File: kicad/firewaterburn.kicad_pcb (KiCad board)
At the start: 4 copper layers, 90 x 50 mm, 83 parts, among them J201 AudioJack2_SwitchT, J202 AudioJack2_SwitchT, J203 AudioJack2_SwitchT, J204 AudioJack2_SwitchT, J205 AudioJack2_SwitchT, J206 AudioJack2_SwitchT, J207 Conn_01x03, J301 Conn_01x05, J302 TC-2050, J501 RVT50HQBNWC00, P101 USB_C_Plug_USB2.0, Q201 DMP31D0U-7, Q202 DMN61D9UWQ-13, Q401 SI7421DN-T1-E3, U101 TPD4E02B04DQA, U301 BL654, U401 LT3973-3.3, U402 STUSB4500QTR, U403 LM2775DSG, Y301 Crystal

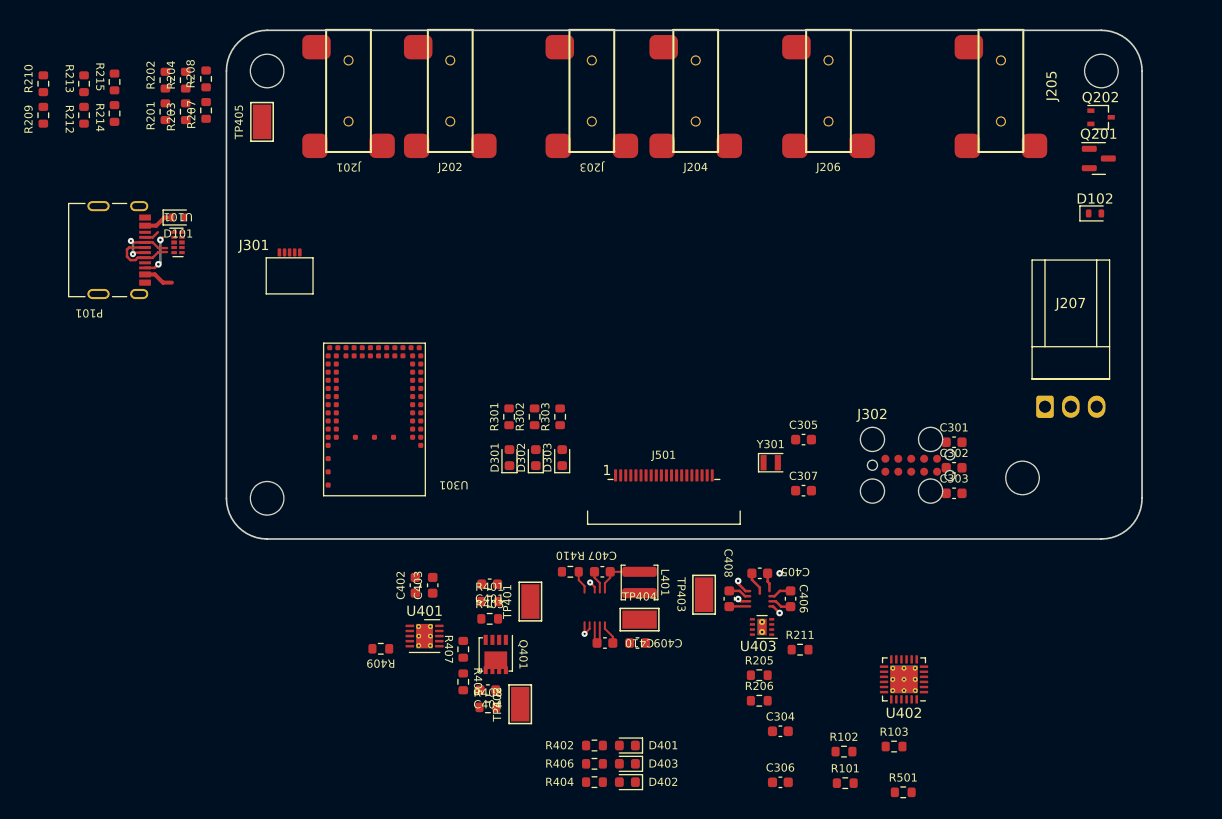
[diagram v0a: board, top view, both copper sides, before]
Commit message: add nrf52840 board
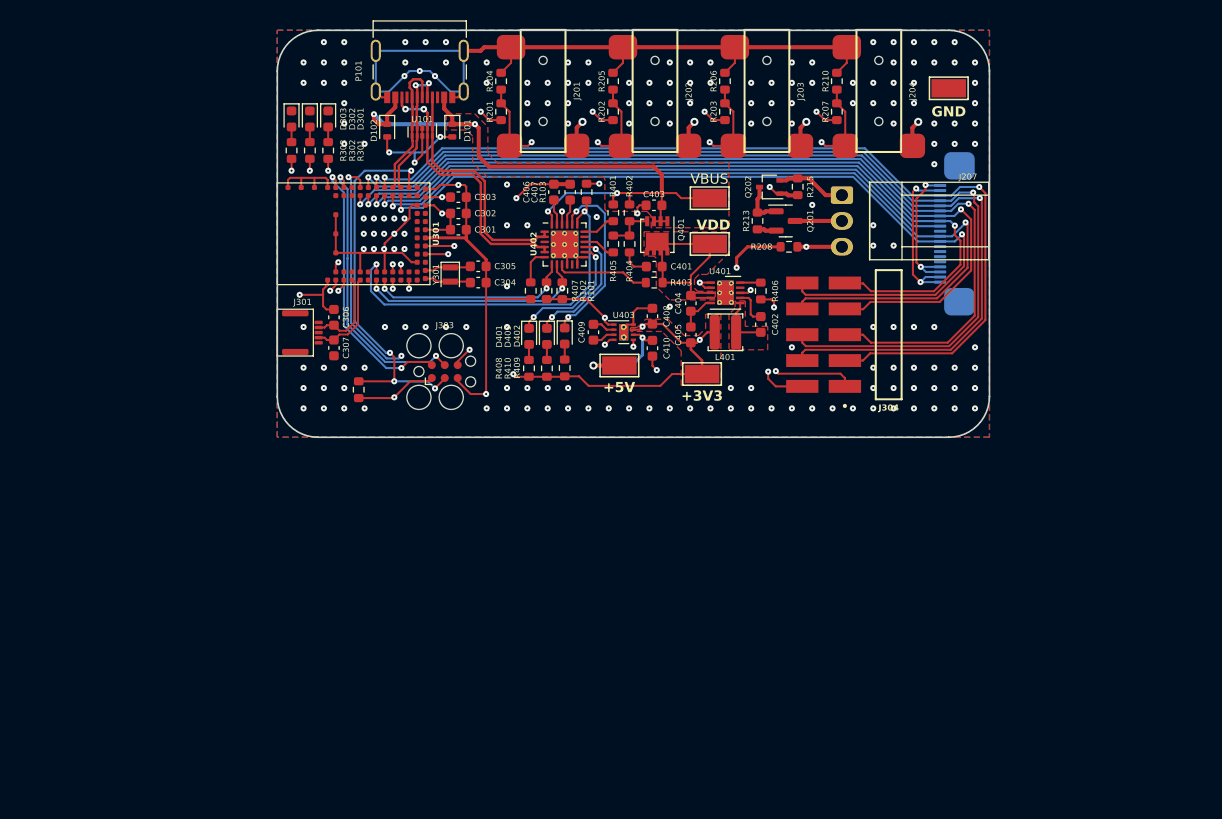
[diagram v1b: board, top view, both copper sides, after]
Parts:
- removed J205, J206: AudioJack2_SwitchT, mylib_connector:MJ-2523
- removed J302: TC-2050, mylib_connector:TC-2050
- removed R209: 4k42, Resistor_SMD:R_0603_1608Metric
- removed R211, R212: 3k4, Resistor_SMD:R_0603_1608Metric
- removed R214: 10k, Resistor_SMD:R_0603_1608Metric
- removed R501: 0R, Resistor_SMD:R_0603_1608Metric
- added J303: Conn_ARM_SWD_TagConnect_TC2030, Connector:Tag-Connect_TC2030-IDC-FP_2x03_P1.27mm_Vertical, F.Cu at (116.5, 93.5)
- added J304: TSM-105-01-L-DH, mylib_connector:SAMTEC_TSM-105-01-L-DH, F.Cu at (160.1, 89.9)
- added R305: 4k7, Resistor_SMD:R_0603_1608Metric, F.Cu at (108.0, 95.3)
- J501: moved to B.Cu
- R208: value 4k42 -> 4k7
- U301: footprint mylib_ic:BL654 -> mylib_ic:BL654-00001
- moved R210 78.0 mm to (155.0, 65.0)
- moved D102 70.1 mm to (110.8, 69.8), turned to -90 degrees
- moved R215 67.9 mm to (151.2, 75.4)
- moved R213 67.6 mm to (147.2, 78.7)
- moved TP401 65.1 mm to (166.0, 65.7), turned to 0 degrees
- moved C306 63.4 mm to (105.6, 88.2), turned to 90 degrees
- moved R103 62.3 mm to (130.4, 75.9), turned to -90 degrees
- moved R207 62.0 mm to (155.0, 68.0)
- moved R206 61.0 mm to (144.0, 65.0), turned to 90 degrees
- moved R205 60.1 mm to (133.0, 65.0), turned to 90 degrees
- moved R208 59.6 mm to (150.3, 81.3), turned to 0 degrees
- moved C303 56.8 mm to (117.8, 76.4)
- moved R101 55.8 mm to (128.0, 85.6), turned to 90 degrees
- moved C302 54.8 mm to (117.8, 78.0)
- moved U402 54.2 mm to (128.2, 81.0), turned to 0 degrees
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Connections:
- net Net-(J301-Pin_2) renamed /mcu_n_tft/NFC+
- net Net-(J301-Pin_4) renamed /mcu_n_tft/NFC-
- J501 pad 1: Net-(J501-VDD) -> +3V3
- J501 pad 17: Net-(J501-VDD) -> +3V3
- J501 pad 18: Net-(J501-VDD) -> +3V3
- R208 pad 2: /OUTPUT/probe4 -> /OUTPUT/TACHO
- R301 pad 2: Net-(U301-P0.17) -> /mcu_n_tft/LED1
- R302 pad 2: Net-(U301-P0.15) -> /mcu_n_tft/LED2
- R303 pad 2: Net-(U301-P0.13) -> /mcu_n_tft/LED3
- U301 pad 10: unconnected-(U301-P0.24-Pad10) -> /mcu_n_tft/~{INT}
- U301 pad 11: unconnected-(U301-P0.22-Pad11) -> /mcu_n_tft/QSPI_IO1
- U301 pad 12: unconnected-(U301-P0.21-Pad12) -> /mcu_n_tft/~{PD}
- U301 pad 13: unconnected-(U301-P0.20-Pad13) -> /mcu_n_tft/QSPI_CLK
- U301 pad 14: unconnected-(U301-P0.19-Pad14) -> /mcu_n_tft/GPIO0
- U301 pad 16: Net-(U301-P0.17) -> /mcu_n_tft/QSPI_IO2
- U301 pad 18: Net-(U301-P0.15) -> /mcu_n_tft/QSPI_IO3
- U301 pad 19: /mcu_n_tft/Reset -> /mcu_n_tft/~{Reset}
- U301 pad 2: /mcu_n_tft/SCL -> unconnected-(U301-P1.04-Pad2)
- U301 pad 20: Net-(U301-P0.13) -> unconnected-(U301-P0.13-Pad20)
- U301 pad 21: /mcu_n_tft/GPIO0 -> unconnected-(U301-P0.16-Pad21)
- U301 pad 22: /mcu_n_tft/~{PD} -> unconnected-(U301-P0.14-Pad22)
- U301 pad 27: /mcu_n_tft/~{INT} -> unconnected-(U301-P0.11-Pad27)
- U301 pad 28: /mcu_n_tft/QSPI_CLK -> unconnected-(U301-P0.12-Pad28)
- U301 pad 29: /mcu_n_tft/QSPI_~{CS} -> unconnected-(U301-P0.08-Pad29)
- U301 pad 30: /mcu_n_tft/I2C_INT -> unconnected-(U301-P1.09-Pad30)
- U301 pad 34: /OUTPUT/probe3 -> /OUTPUT/probe4
- U301 pad 35: /mcu_n_tft/QSPI_IO3 -> /OUTPUT/PWM
- U301 pad 36: /mcu_n_tft/QSPI_IO2 -> unconnected-(U301-P0.26-Pad36)
- U301 pad 37: /mcu_n_tft/QSPI_IO1 -> /OUTPUT/TACHO
- U301 pad 38: /mcu_n_tft/QSPI_IO0 -> unconnected-(U301-P0.27-Pad38)
- U301 pad 39: /OUTPUT/probe4 -> /OUTPUT/probe5
- U301 pad 4: /mcu_n_tft/SDA -> unconnected-(U301-P1.02-Pad4)
- U301 pad 44: /mcu_n_tft/ADC_7 -> /OUTPUT/probe7
- U301 pad 45: /OUTPUT/probe7 -> /OUTPUT/probe3
- U301 pad 46: /OUTPUT/probe5 -> /OUTPUT/probe6
- U301 pad 48: /OUTPUT/probe6 -> /OUTPUT/probe1
- U301 pad 5: /OUTPUT/TACHO -> unconnected-(U301-P1.03-Pad5)
- U301 pad 50: /OUTPUT/probe1 -> /OUTPUT/probe0
- U301 pad 51: unconnected-(U301-P1.14-Pad51) -> /mcu_n_tft/SCL
- U301 pad 53: unconnected-(U301-P1.15-Pad53) -> /mcu_n_tft/SDA
- U301 pad 54: unconnected-(U301-P1.12-Pad54) -> /mcu_n_tft/I2C_INT
- U301 pad 6: /OUTPUT/PWM -> unconnected-(U301-P1.01-Pad6)
- U301 pad 61: unconnected-(U301-P1.05-Pad61) -> /mcu_n_tft/LED3
- U301 pad 63: unconnected-(U301-P1.06-Pad63) -> /mcu_n_tft/LED2
- U301 pad 64: unconnected-(U301-P1.07-Pad64) -> /mcu_n_tft/LED1
- U301 pad 8: unconnected-(U301-P0.25-Pad8) -> /mcu_n_tft/QSPI_~{CS}
- U301 pad 9: unconnected-(U301-P0.23-Pad9) -> /mcu_n_tft/QSPI_IO0
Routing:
- net GND: track 9.05 -> 240.5 mm, vias 0 -> 194
- net +3V3: track 29.3 -> 231.3 mm, vias 6 -> 19
- net /mcu_n_tft/QSPI_IO0: track 0.00 -> 96.8 mm, vias 0 -> 2
- net /mcu_n_tft/QSPI_IO1: track 0.00 -> 95.3 mm, vias 0 -> 2
- net /mcu_n_tft/QSPI_CLK: track 0.00 -> 91.9 mm, vias 0 -> 2
- net /mcu_n_tft/QSPI_~{CS}: track 0.00 -> 90.3 mm, vias 0 -> 2
- net /mcu_n_tft/QSPI_IO2: track 0.00 -> 84.8 mm, vias 0 -> 2
- net /mcu_n_tft/~{INT}: track 0.00 -> 83.6 mm, vias 0 -> 2
- net /mcu_n_tft/QSPI_IO3: track 0.00 -> 82.0 mm, vias 0 -> 2
- net /mcu_n_tft/~{PD}: track 0.00 -> 78.5 mm, vias 0 -> 2
- net VBUS: track 5.93 -> 69.0 mm, vias 0 -> 4
- net /OUTPUT/probe3: track 0.00 -> 61.1 mm, vias 0 -> 2
- net /mcu_n_tft/GPIO0: track 0.00 -> 59.2 mm, vias 0 -> 1
- net /mcu_n_tft/SDA: track 0.00 -> 54.9 mm, vias 0 -> 3
- net /OUTPUT/probe2: track 0.00 -> 51.1 mm, vias 0 -> 2
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- added copper zone on F.Cu, net +3V3
- added copper zone on In2.Cu, net +3V3
- added copper zone on B.Cu, net GND
- added copper zone on F.Cu, net GND
- added copper zone on In1.Cu, net GND
- added copper zone on In2.Cu, net GND
- added copper zone on F.Cu, net Net-(U401-SW)
- added copper zone on F.Cu, net VBUS
- added copper zone on F.Cu, net VDD
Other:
- board size 90 x 50 mm -> 70 x 40 mm
- board text added: "+3V3"
- board text added: "+5V"
- board text added: "GND"
- board text added: "VBUS"
- board text added: "VDD"

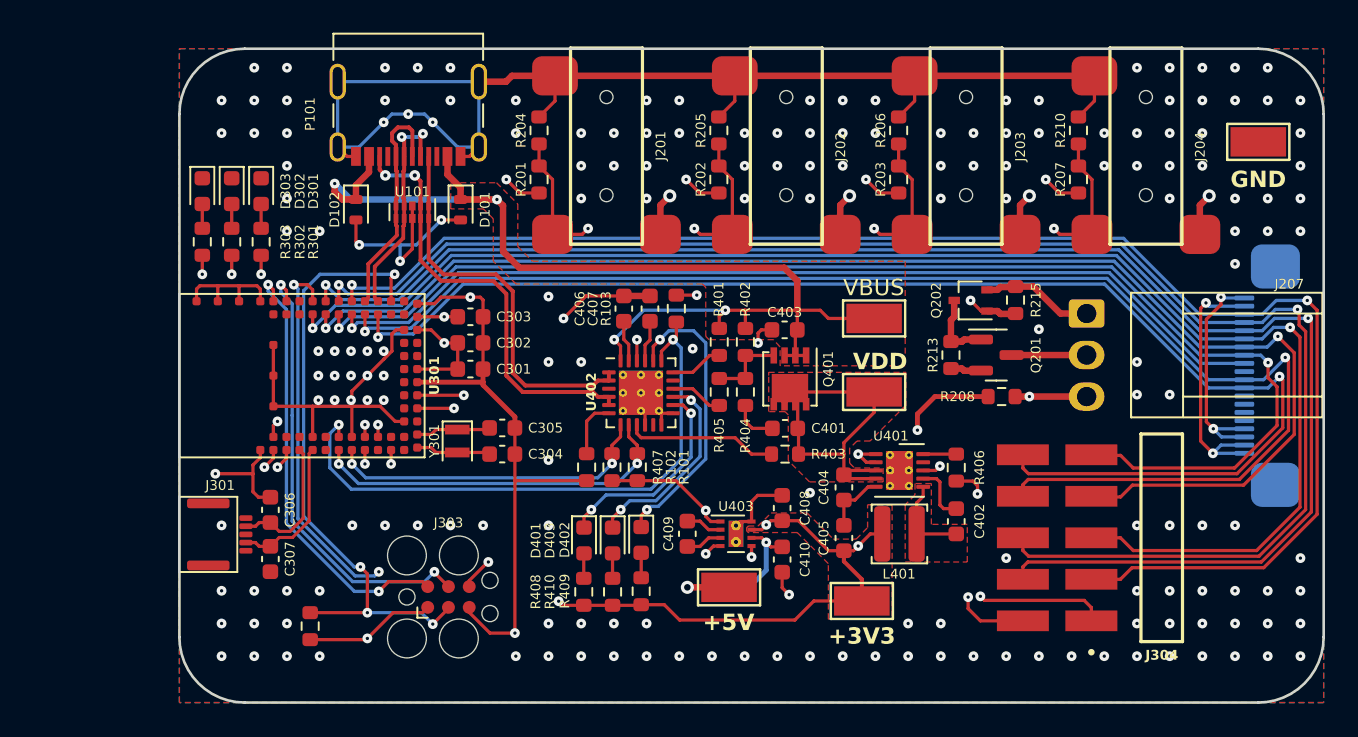
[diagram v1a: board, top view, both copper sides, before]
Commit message: rework board
add nrf 7002
add oled display
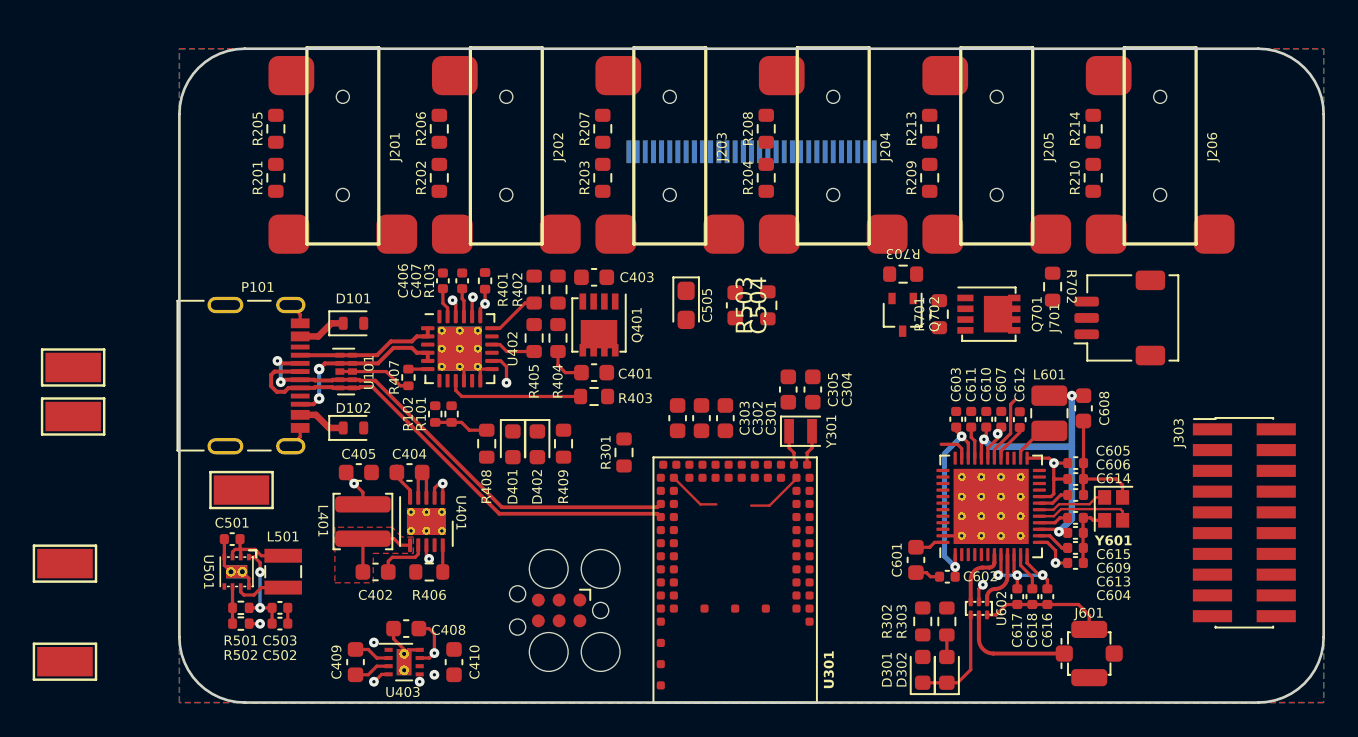
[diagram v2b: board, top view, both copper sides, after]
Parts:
- removed C306, C307: 300p, Capacitor_SMD:C_0603_1608Metric
- removed D303, D403: LED, LED_SMD:LED_0603_1608Metric
- removed J207: Conn_01x03, mylib_connector:Molex_KK-254_AE-6410-03A_1x03_P2.54mm_Vertical
- removed J304: TSM-105-01-L-DH, mylib_connector:SAMTEC_TSM-105-01-L-DH
- removed Q201: DMP31D0U-7, Package_TO_SOT_SMD:SOT-23
- removed Q202: DMN61D9UWQ-13, Package_TO_SOT_SMD:SOT-323_SC-70
- removed R215, R305: 4k7, Resistor_SMD:R_0603_1608Metric
- removed R410: 1k, Resistor_SMD:R_0603_1608Metric
- added C501: 1µ, Capacitor_SMD:C_0402_1005Metric, F.Cu at (103.2, 90.0)
- added C502: 10µ, Capacitor_SMD:C_0402_1005Metric, F.Cu at (106.2, 95.2)
- added C503: 100nF, Capacitor_SMD:C_0402_1005Metric, F.Cu at (106.2, 94.2)
- added C504: 100nF, Capacitor_SMD:C_0603_1608Metric, F.Cu at (134.0, 75.7)
- added C505: 4µ7, Capacitor_Tantalum_SMD:CP_EIA-2012-15_AVX-P, F.Cu at (131.0, 75.7)
- added C601: 2µ2, Capacitor_SMD:C_0603_1608Metric, F.Cu at (145.1, 91.3)
- added C602: 100n, Capacitor_SMD:C_0402_1005Metric, F.Cu at (147.0, 92.3)
- added C603: 2µ2, Capacitor_SMD:C_0402_1005Metric, F.Cu at (147.5, 82.7)
- added C604: 4µ7, Capacitor_SMD:C_0402_1005Metric, F.Cu at (154.8, 91.5)
- added C605: 4µ7, Capacitor_SMD:C_0402_1005Metric, F.Cu at (154.8, 85.3)
- added C606: 1µ, Capacitor_SMD:C_0402_1005Metric, F.Cu at (154.8, 86.3)
- added C607: 2µ2, Capacitor_SMD:C_0402_1005Metric, F.Cu at (150.3, 82.7)
- added C608: 4µ7, Capacitor_SMD:C_0603_1608Metric, F.Cu at (155.3, 82.0)
- added C609: 0.22µ, Capacitor_SMD:C_0402_1005Metric, F.Cu at (154.8, 89.6)
- added C610: 0.47µ, Capacitor_SMD:C_0402_1005Metric, F.Cu at (149.4, 82.7)
- added C611: 1µ, Capacitor_SMD:C_0402_1005Metric, F.Cu at (148.4, 82.7)
- added C612: 10n, Capacitor_SMD:C_0402_1005Metric, F.Cu at (151.4, 82.7)
- added C613: 22n, Capacitor_SMD:C_0402_1005Metric, F.Cu at (154.8, 90.5)
- added C614: 1µ, Capacitor_SMD:C_0402_1005Metric, F.Cu at (154.8, 87.3)
- added C615: 2µ2, Capacitor_SMD:C_0402_1005Metric, F.Cu at (154.8, 88.7)
- added C616: 4µ7, Capacitor_SMD:C_0402_1005Metric, F.Cu at (153.1, 93.5)
- added C617: 100n, Capacitor_SMD:C_0402_1005Metric, F.Cu at (151.3, 93.5)
- added C618: 0.47µ, Capacitor_SMD:C_0402_1005Metric, F.Cu at (152.2, 93.5)
- added J205: AudioJack2_SwitchT, mylib_connector:MJ-2523, F.Cu at (150.0, 59.9)
- added J206: AudioJack2_SwitchT, mylib_connector:MJ-2523, F.Cu at (160.0, 59.9)
- added J601: Conn_Coaxial, mylib_connector:CONMHF1-SMD-G-T, F.Cu at (155.7, 97.0)
- added J701: Conn_01x03, mylib_connector:Molex_Pico-Clasp_202396-0307_1x03-1MP_P1.00mm_Horizontal, F.Cu at (157.5, 76.5)
- added L501: 10µ, Inductor_SMD:L_Wuerth_MAPI-2510, F.Cu at (106.3, 92.0)
- added L601: 3µ3, Inductor_SMD:L_1008_2520Metric, F.Cu at (153.2, 82.3)
- added Q701: SI7421DN-T1-E3, mylib_ic:Vishay_PowerPAK_1212-8_Single, F.Cu at (149.5, 76.2)
- added Q702: DMN61D9UWQ-13, Package_TO_SOT_SMD:SOT-323_SC-70, F.Cu at (144.2, 76.3)
- added R209: 4k42, Resistor_SMD:R_0603_1608Metric, F.Cu at (145.9, 67.9)
- added R214: 3k4, Resistor_SMD:R_0603_1608Metric, F.Cu at (155.9, 64.9)
- added R501: 47k5, Resistor_SMD:R_0402_1005Metric, F.Cu at (103.8, 94.2)
- added R502: 5k, Resistor_SMD:R_0402_1005Metric, F.Cu at (103.8, 95.2)
- added R503: 910k, Resistor_SMD:R_0603_1608Metric, F.Cu at (136.0, 75.7)
- added R701: 4k7, Resistor_SMD:R_0603_1608Metric, F.Cu at (146.5, 76.2)
- added R702: 4k7, Resistor_SMD:R_0603_1608Metric, F.Cu at (153.4, 74.6)
- added R703: 4k7, Resistor_SMD:R_0603_1608Metric, F.Cu at (144.3, 73.8)
- added U501: MIC2290, mylib_ic:Micrel_MLF-8-1EP_2x2mm_P0.5mm_EP0.8x1.3mm_ThermalVias, F.Cu at (103.5, 92.0)
- added U601: NRF7002-QFAA-Rx, Package_DFN_QFN:QFN-48-1EP_6x6mm_P0.4mm_EP4.6x4.6mm_ThermalVias, F.Cu at (149.7, 88.0)
- added U602: ~, mylib_connector:DPX1608LL80R2455A, F.Cu at (148.9, 94.2)
- added Y601: 40MHz, Crystal:Crystal_SMD_2016-4Pin_2.0x1.6mm, F.Cu at (157.2, 88.2)
- C406, C407: footprint Capacitor_SMD:C_0603_1608Metric -> Capacitor_SMD:C_0402_1005Metric
- J301: value Conn_01x05 -> Conn_ARM_SWD_TagConnect_TC2030; footprint mylib_connector:Easy-On 51281-5 -> Connector:Tag-Connect_TC2030-IDC-FP_2x03_P1.27mm_Vertical
- J303: value Conn_ARM_SWD_TagConnect_TC2030 -> Conn_02x10_Odd_Even; footprint Connector:Tag-Connect_TC2030-IDC-FP_2x03_P1.27mm_Vertical -> Connector_PinHeader_1.27mm:PinHeader_2x10_P1.27mm_Vertical_SMD
- J501: value RVT50HQBNWC00 -> EA W128064-XALG; footprint mylib_connector:FPC_BOTTOM_20POS_Würth_68712014522 -> mylib_connector:SFV31R-4STE1HLF
- Q401: footprint Package_SO:Vishay_PowerPAK_1212-8_Single -> mylib_ic:Vishay_PowerPAK_1212-8_Single
- R101, R102, R103, R407: footprint Resistor_SMD:R_0603_1608Metric -> Resistor_SMD:R_0402_1005Metric
- R204, R210: value 3k4 -> 4k42
- R207: value 4k42 -> 3k4
- R208, R213: value 4k7 -> 3k4
- R301: value 1k -> 4k7
- moved TP401 65.7 mm to (103.8, 87.0)
- moved D302 52.6 mm to (146.9, 98.0), turned to 90 degrees
- moved R303 51.1 mm to (146.9, 95.0), turned to 90 degrees
- moved D301 50.0 mm to (145.5, 98.0), turned to 90 degrees
- moved TP402 49.1 mm to (93.5, 79.5)
- moved TP403 49.0 mm to (93.5, 82.5)
- moved J303 48.9 mm to (165.2, 89.0)
- moved TP404 48.8 mm to (93.0, 91.5)
- moved R302 48.2 mm to (145.5, 95.0), turned to 90 degrees
- moved TP405 40.9 mm to (93.0, 97.5)
- moved C402 35.7 mm to (112.0, 92.0), turned to 180 degrees
- moved R406 32.9 mm to (115.3, 92.0), turned to 180 degrees
- moved J501 32.8 mm to (135.0, 67.0), turned to 180 degrees
- moved L401 32.8 mm to (111.2, 88.9), turned to 90 degrees
- moved C405 29.9 mm to (111.0, 85.9), turned to 0 degrees
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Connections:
- J301 pad 1: unconnected-(J301-Pin_1-Pad1) -> +3V3
- J301 pad 2: /mcu_n_tft/NFC+ -> /mcu_n_tft/SWDIO
- J301 pad 3: unconnected-(J301-Pin_3-Pad3) -> /mcu_n_tft/~{Reset}
- J301 pad 4: /mcu_n_tft/NFC- -> /mcu_n_tft/SWCLK
- J301 pad 5: unconnected-(J301-Pin_5-Pad5) -> GND
- J303 pad 1: +3V3 -> /mcu_n_tft/UART_TX
- J303 pad 2: /mcu_n_tft/SWDIO -> /mcu_n_tft/UART_RX
- J303 pad 3: /mcu_n_tft/~{Reset} -> /mcu_n_tft/SDA
- J303 pad 4: /mcu_n_tft/SWCLK -> /mcu_n_tft/SCL
- J303 pad 5: GND -> /mcu_n_tft/QSPI_CLK
- J303 pad 6: /mcu_n_tft/SWO -> /mcu_n_tft/QSPI_IO0
- J501 pad 1: +3V3 -> GND
- J501 pad 11: /mcu_n_tft/QSPI_IO2 -> +3V3
- J501 pad 12: /mcu_n_tft/QSPI_IO3 -> GND
- J501 pad 13: unconnected-(J501-Pad13) -> GND
- J501 pad 15: unconnected-(J501-Pad15) -> /mcu_n_tft/TFT_~{CS}
- J501 pad 16: unconnected-(J501-Pad16) -> /mcu_n_tft/TFT_~{RESET}
- J501 pad 17: +3V3 -> /mcu_n_tft/TFT_D/C
- J501 pad 18: +3V3 -> GND
- J501 pad 20: GND -> /mcu_n_tft/TFT_CLK
- J501 pad 3: /mcu_n_tft/QSPI_CLK -> unconnected-(J501-Pad3)
- J501 pad 4: /mcu_n_tft/QSPI_IO1 -> unconnected-(J501-Pad4)
- J501 pad 5: /mcu_n_tft/QSPI_IO0 -> unconnected-(J501-Pad5)
- J501 pad 6: /mcu_n_tft/QSPI_~{CS} -> unconnected-(J501-Pad6)
- J501 pad 7: /mcu_n_tft/~{INT} -> unconnected-(J501-Pad7)
- J501 pad 8: /mcu_n_tft/~{PD} -> unconnected-(J501-Pad8)
- J501 pad 9: /mcu_n_tft/GPIO0 -> unconnected-(J501-Pad9)
- R204 pad 1: /OUTPUT/probe0 -> +3V3
- R204 pad 2: GND -> /OUTPUT/probe3
- R205 pad 1: /OUTPUT/probe1 -> /OUTPUT/probe0
- R206 pad 1: /OUTPUT/probe2 -> /OUTPUT/probe1
- R207 pad 1: +3V3 -> /OUTPUT/probe2
- R207 pad 2: /OUTPUT/probe3 -> GND
- R208 pad 1: +3V3 -> /OUTPUT/probe3
- R208 pad 2: /OUTPUT/TACHO -> GND
- R210 pad 1: /OUTPUT/probe3 -> +3V3
- R210 pad 2: GND -> /OUTPUT/probe5
- R213 pad 1: +12V -> /OUTPUT/probe4
- R213 pad 2: Net-(Q201-G) -> GND
- R301 pad 1: Net-(D301-A) -> +3V3
- R301 pad 2: /mcu_n_tft/LED1 -> /mcu_n_tft/~{Reset}
- R302 pad 1: Net-(D302-A) -> Net-(D301-A)
- R302 pad 2: /mcu_n_tft/LED2 -> /mcu_n_tft/LED1
- R303 pad 1: Net-(D303-A) -> Net-(D302-A)
- R303 pad 2: /mcu_n_tft/LED3 -> /mcu_n_tft/LED2
- U301 pad 10: /mcu_n_tft/~{INT} -> /mcu_n_tft/COEX_REQ
- U301 pad 12: /mcu_n_tft/~{PD} -> /mcu_n_tft/COEX_STATUS
- U301 pad 14: /mcu_n_tft/GPIO0 -> /mcu_n_tft/BUCKEN
- U301 pad 20: unconnected-(U301-P0.13-Pad20) -> /mcu_n_tft/COEX_GRANT
- U301 pad 22: unconnected-(U301-P0.14-Pad22) -> /mcu_n_tft/SW_CTRL1
- U301 pad 35: /OUTPUT/PWM -> /fan_control/PWM
- U301 pad 37: /OUTPUT/TACHO -> /fan_control/TACHO
- U301 pad 57: /mcu_n_tft/NFC- -> unconnected-(U301-NFC_2-Pad57)
- U301 pad 59: /mcu_n_tft/NFC+ -> unconnected-(U301-NFC_1-Pad59)
- U301 pad 60: unconnected-(U301-P1.11-Pad60) -> /mcu_n_tft/BUTTON1
- U301 pad 61: /mcu_n_tft/LED3 -> /mcu_n_tft/IRQ
- U301 pad 62: unconnected-(U301-P1.10-Pad62) -> /mcu_n_tft/BUTTON2
- U402 pad 15: /pwr_supply/GPIO -> unconnected-(U402-GPIO-Pad15)
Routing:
- net GND: track 240.5 -> 51.8 mm, vias 194 -> 2
- net +3V3: track 231.3 -> 48.1 mm, vias 19 -> 11
- net /mcu_n_tft/QSPI_IO0: track 96.8 -> 0.00 mm, vias 2 -> 0
- net /mcu_n_tft/QSPI_IO1: track 95.3 -> 0.00 mm, vias 2 -> 0
- net /mcu_n_tft/QSPI_~{CS}: track 90.3 -> 0.00 mm, vias 2 -> 0
- net /mcu_n_tft/QSPI_CLK: track 91.9 -> 1.96 mm, vias 2 -> 0
- net /mcu_n_tft/QSPI_IO2: track 84.8 -> 0.00 mm, vias 2 -> 0
- net /mcu_n_tft/~{INT}: track 83.6 -> 0.00 mm, vias 2 -> 0
- net /mcu_n_tft/QSPI_IO3: track 82.0 -> 0.00 mm, vias 2 -> 0
- net /mcu_n_tft/~{PD}: track 78.5 -> 0.00 mm, vias 2 -> 0
- net VBUS: track 69.0 -> 5.93 mm, vias 4 -> 0
- net /OUTPUT/probe3: track 61.1 -> 0.00 mm, vias 2 -> 0
- net /mcu_n_tft/GPIO0: track 59.2 -> 0.00 mm, vias 1 -> 0
- net /mcu_n_tft/SDA: track 54.9 -> 0.00 mm, vias 3 -> 0
- net /OUTPUT/probe2: track 51.1 -> 0.00 mm, vias 2 -> 0
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- removed copper zone on F.Cu, net +3V3
- removed copper zone on In2.Cu, net GND
- removed copper zone on F.Cu, net VBUS
- removed copper zone on F.Cu, net VDD
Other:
- board text added: "ABC"
- board text removed: "+3V3"
- board text removed: "+5V"
- board text removed: "GND"
- board text removed: "VBUS"
- board text removed: "VDD"
